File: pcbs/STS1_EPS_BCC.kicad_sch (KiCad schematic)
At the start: 45 parts, among them Q1 SI7135DP-T1-GE3, U1 LTC4020EUHFPBF, U2 SI7272DP-T1-GE3, U3 SI7272DP-T1-GE3

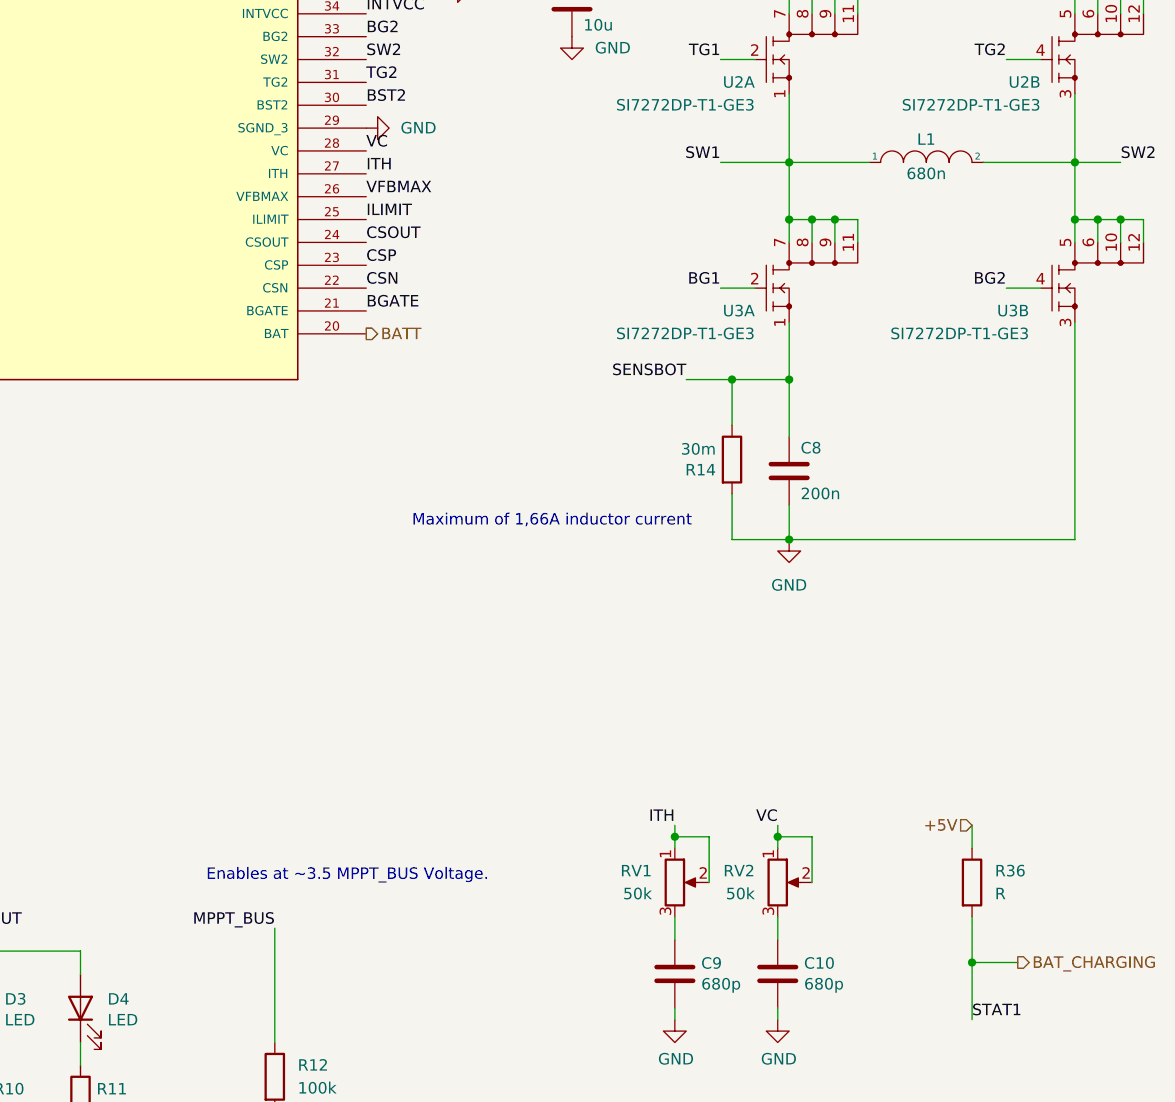
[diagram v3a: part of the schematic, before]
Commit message: Worked on STS1_EPS_1 and began work on STS1_EPS_2.
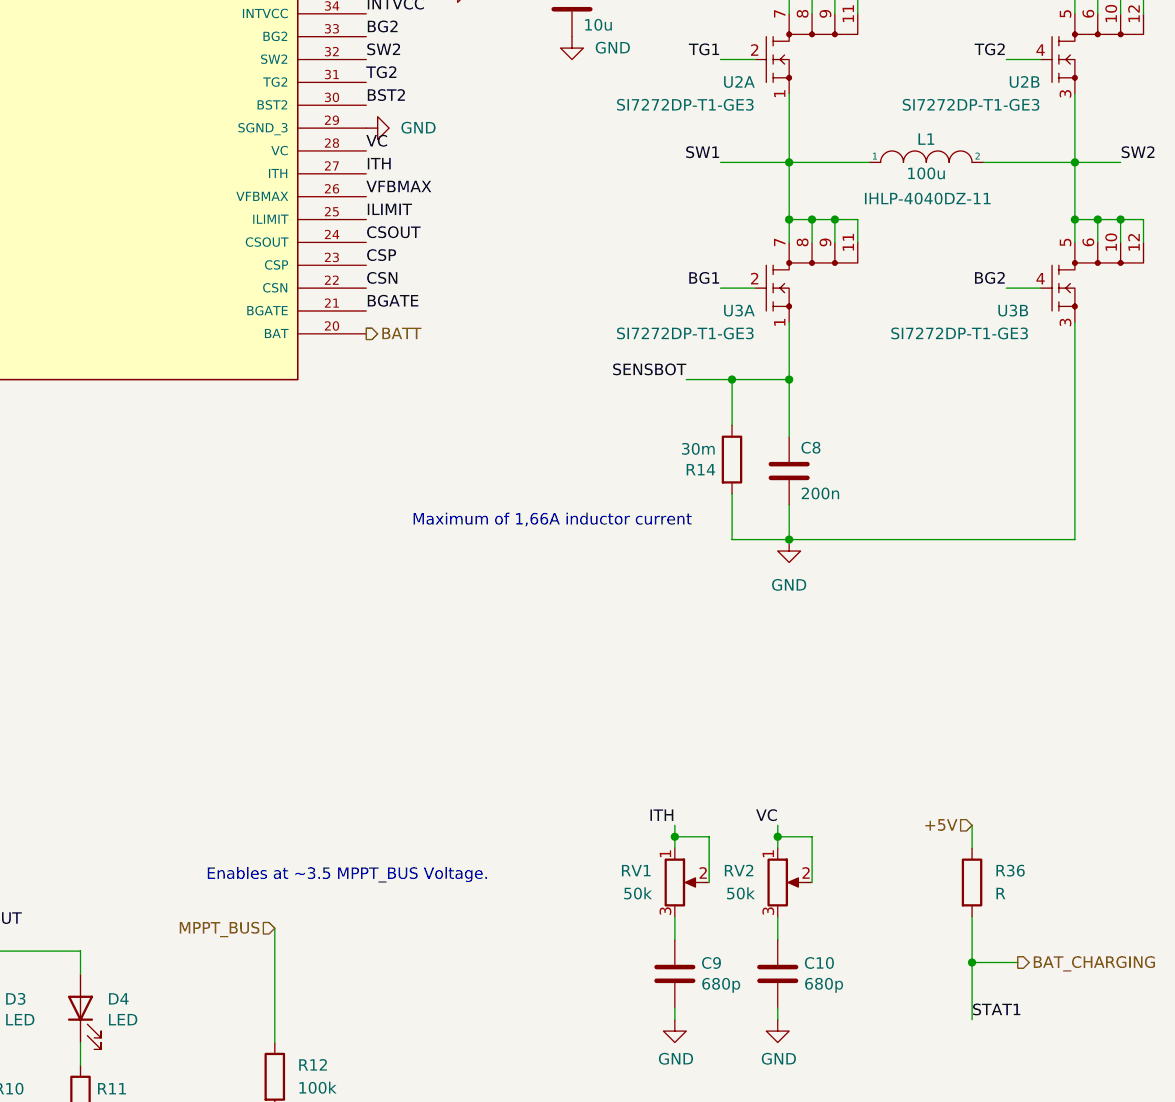
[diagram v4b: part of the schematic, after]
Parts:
- C32, C4: footprint (none) -> Capacitor_Tantalum_SMD:CP_EIA-7343-43_Kemet-X
- L1: value 680n -> 100u; footprint Inductor_SMD:L_10.4x10.4_H4.8 -> Inductor_SMD:L_Vishay_IHLP-4040; Part (none) -> IHLP-4040DZ-11
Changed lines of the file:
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@@
-    (effects (font (size 1.27 1.27)) (justify right bottom))
-  )
-  (label "MPPT_BUS" (at 135.89 148.59 180)
     (effects (font (size 1.27 1.27)) (justify right bottom))
   )
@@
   (label "VFBMAX" (at 146.05 67.31 0)
     (effects (font (size 1.27 1.27)) (justify left bottom))
+  )
+  (hierarchical_label "MPPT_BUS" (shape input) (at 135.89 148.59 180)
+    (effects (font (size 1.27 1.27)) (justify right))
   )
   (hierarchical_label "VOUT" (shape output) (at 275.59 16.51 0)
@@
     (in_bom yes) (on_board yes)
     (property "Reference" "L1" (id 0) (at 208.28 60.96 0))
-    (property "Value" "680n" (id 1) (at 208.28 64.77 0))
-    (property "Footprint" "Inductor_SMD:L_10.4x10.4_H4.8" (id 2) (at 208.28 63.5 0)
+    (property "Value" "100u" (id 1) (at 208.28 64.77 0))
+    (property "Footprint" "Inductor_SMD:L_Vishay_IHLP-4040" (id 2) (at 208.28 63.5 0)
       (effects (font (size 1.27 1.27)) hide)
     )
@@
       (effects (font (size 1.27 1.27)) hide)
     )
+    (property "Part" "IHLP-4040DZ-11" (id 4) (at 208.4324 67.564 0))
     (pin "1")
     (pin "2")
@@
       (effects (font (size 1.27 1.27)) (justify left))
     )
-    (property "Footprint" "" (id 2) (at 237.1852 24.13 0)
+    (property "Footprint" "Capacitor_Tantalum_SMD:CP_EIA-7343-43_Kemet-X" (id 2) (at 237.1852 24.13 0)
       (effects (font (size 1.27 1.27)) hide)
     )
@@
       (effects (font (size 1.27 1.27)) (justify left))
     )
-    (property "Footprint" "" (id 2) (at 33.9852 27.94 0)
-      (effects (font (size 1.27 1.27)) hide)
-    )
+    (property "Footprint" "Capacitor_Tantalum_SMD:CP_EIA-7343-43_Kemet-X" (id 2) (at 33.9852 27.94 0)
+      (effects (font (size 1.27 1.27)) hide)
+    )

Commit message: Finished first revision of schematic.
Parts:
- added R?: 100k, Resistor_SMD:R_0805_2012Metric, symbol Device:R
- R36: value R -> 100k
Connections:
- net +5V: now also R?.1
- net STAT2 renamed BAT_FAULT
- net BAT_FAULT: now also R?.2
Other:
- moved on the sheet: C33
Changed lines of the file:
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@@
   (junction (at 102.87 151.13) (diameter 0) (color 0 0 0 0)
   )
+  (junction (at 236.22 152.4) (diameter 0) (color 0 0 0 0)
+  )
   (junction (at 229.87 44.45) (diameter 0) (color 0 0 0 0)
   )
@@
     (stroke (width 0) (type default) (color 0 0 0 0))
   )
+  (wire (pts (xy 236.22 147.32) (xy 236.22 152.4))
+    (stroke (width 0) (type default) (color 0 0 0 0))
+  )
   (wire (pts (xy 270.51 36.83) (xy 273.05 36.83))
     (stroke (width 0) (type default) (color 0 0 0 0))
@@
     (stroke (width 0) (type default) (color 0 0 0 0))
   )
+  (wire (pts (xy 236.22 152.4) (xy 241.3 152.4))
+    (stroke (width 0) (type default) (color 0 0 0 0))
+  )
   (wire (pts (xy 265.43 34.29) (xy 267.97 34.29))
     (stroke (width 0) (type default) (color 0 0 0 0))
@@
     (stroke (width 0) (type default) (color 0 0 0 0))
   )
-  (wire (pts (xy 248.92 137.16) (xy 248.92 144.78))
+  (wire (pts (xy 271.78 137.16) (xy 271.78 144.78))
     (stroke (width 0) (type default) (color 0 0 0 0))
   )
@@
     (stroke (width 0) (type default) (color 0 0 0 0))
   )
-  (wire (pts (xy 248.92 152.4) (xy 248.92 158.75))
+  (wire (pts (xy 271.78 152.4) (xy 271.78 158.75))
     (stroke (width 0) (type default) (color 0 0 0 0))
   )
@@
     (stroke (width 0) (type default) (color 0 0 0 0))
   )
+  (wire (pts (xy 236.22 152.4) (xy 236.22 158.75))
+    (stroke (width 0) (type default) (color 0 0 0 0))
+  )
   (wire (pts (xy 39.37 173.99) (xy 39.37 175.26))
     (stroke (width 0) (type default) (color 0 0 0 0))
@@
   )
   (wire (pts (xy 29.21 173.99) (xy 25.4 173.99))
+    (stroke (width 0) (type default) (color 0 0 0 0))
+  )
+  (wire (pts (xy 236.22 137.16) (xy 236.22 139.7))
     (stroke (width 0) (type default) (color 0 0 0 0))
   )
@@
     (effects (font (size 1.27 1.27)) (justify left bottom))
   )
+  (label "STAT2" (at 236.22 158.75 0)
+    (effects (font (size 1.27 1.27)) (justify left bottom))
+  )
   (label "TG1" (at 185.42 52.07 180)
     (effects (font (size 1.27 1.27)) (justify right bottom))
@@
     (effects (font (size 1.27 1.27)) (justify left bottom))
   )
-  (label "CSOUT" (at 248.92 137.16 180)
+  (label "CSOUT" (at 271.78 137.16 180)
     (effects (font (size 1.27 1.27)) (justify right bottom))
   )
@@
     (effects (font (size 1.27 1.27)) (justify left))
   )
+  (hierarchical_label "BAT_FAULT" (shape output) (at 241.3 152.4 0)
+    (effects (font (size 1.27 1.27)) (justify left))
+  )
   (hierarchical_label "MPPT_BUS" (shape input) (at 25.4 16.51 180)
     (effects (font (size 1.27 1.27)) (justify right))
@@
   )
   (hierarchical_label "NTC" (shape input) (at 74.93 72.39 180)
+    (effects (font (size 1.27 1.27)) (justify right))
+  )
+  (hierarchical_label "+5V" (shape input) (at 236.22 137.16 180)
     (effects (font (size 1.27 1.27)) (justify right))
   )
@@
     )
     (pin "1")
+  )
+  (symbol (lib_id "Device:R") (at 236.22 143.51 0) (unit 1)
+    (in_bom yes) (on_board yes) (fields_autoplaced)
+    (property "Reference" "R?" (id 0) (at 238.76 142.2399 0)
+      (effects (font (size 1.27 1.27)) (justify left))
+    )
+    (property "Value" "100k" (id 1) (at 238.76 144.7799 0)
+      (effects (font (size 1.27 1.27)) (justify left))
+    )
+    (property "Footprint" "Resistor_SMD:R_0805_2012Metric" (id 2) (at 234.442 143.51 90)
+      (effects (font (size 1.27 1.27)) hide)
+    )
+    (property "Datasheet" "~" (id 3) (at 236.22 143.51 0)
+      (effects (font (size 1.27 1.27)) hide)
+    )
+    (pin "1")
+    (pin "2")
   )
   (symbol (lib_id "Device:R") (at 186.69 96.52 0) (unit 1)
@@
     (pin "2")
   )
-  (symbol (lib_id "power:GND") (at 248.92 158.75 0) (unit 1)
-    (in_bom yes) (on_board yes)
-    (property "Reference" "#PWR093" (id 0) (at 248.92 165.1 0)
-      (effects (font (size 1.27 1.27)) hide)
-    )
-    (property "Value" "GND" (id 1) (at 249.047 163.1442 0))
-    (property "Footprint" "" (id 2) (at 248.92 158.75 0)
-      (effects (font (size 1.27 1.27)) hide)
-    )
-    (property "Datasheet" "" (id 3) (at 248.92 158.75 0)
+  (symbol (lib_id "power:GND") (at 271.78 158.75 0) (unit 1)
+    (in_bom yes) (on_board yes)
+    (property "Reference" "#PWR093" (id 0) (at 271.78 165.1 0)
+      (effects (font (size 1.27 1.27)) hide)
+    )
+    (property "Value" "GND" (id 1) (at 271.907 163.1442 0))
+    (property "Footprint" "" (id 2) (at 271.78 158.75 0)
+      (effects (font (size 1.27 1.27)) hide)
+    )
+    (property "Datasheet" "" (id 3) (at 271.78 158.75 0)
       (effects (font (size 1.27 1.27)) hide)
     )
@@
     (pin "2")
   )
-  (symbol (lib_id "Device:C") (at 248.92 148.59 0) (unit 1)
-    (in_bom yes) (on_board yes)
-    (property "Reference" "C33" (id 0) (at 251.841 147.4216 0)
-      (effects (font (size 1.27 1.27)) (justify left))
-    )
-    (property "Value" "100p" (id 1) (at 251.841 149.733 0)
-      (effects (font (size 1.27 1.27)) (justify left))
-    )
-    (property "Footprint" "Capacitor_SMD:C_0805_2012Metric" (id 2) (at 249.8852 152.4 0)
-      (effects (font (size 1.27 1.27)) hide)
-    )
-    (property "Datasheet" "~" (id 3) (at 248.92 148.59 0)
+  (symbol (lib_id "Device:C") (at 271.78 148.59 0) (unit 1)
+    (in_bom yes) (on_board yes)
+    (property "Reference" "C33" (id 0) (at 274.701 147.4216 0)
+      (effects (font (size 1.27 1.27)) (justify left))
+    )
+    (property "Value" "100p" (id 1) (at 274.701 149.733 0)
+      (effects (font (size 1.27 1.27)) (justify left))
+    )
+    (property "Footprint" "Capacitor_SMD:C_0805_2012Metric" (id 2) (at 272.7452 152.4 0)
+      (effects (font (size 1.27 1.27)) hide)
+    )
+    (property "Datasheet" "~" (id 3) (at 271.78 148.59 0)
       (effects (font (size 1.27 1.27)) hide)
     )
@@
       (effects (font (size 1.27 1.27)) (justify left))
     )
-    (property "Value" "R" (id 1) (at 215.9 144.7799 0)
-      (effects (font (size 1.27 1.27)) (justify left))
-    )
+    (property "Value" "100k" (id 1) (at 215.9 144.7799 0)
+      (effects (font (size 1.27 1.27)) (justify left))
+    )

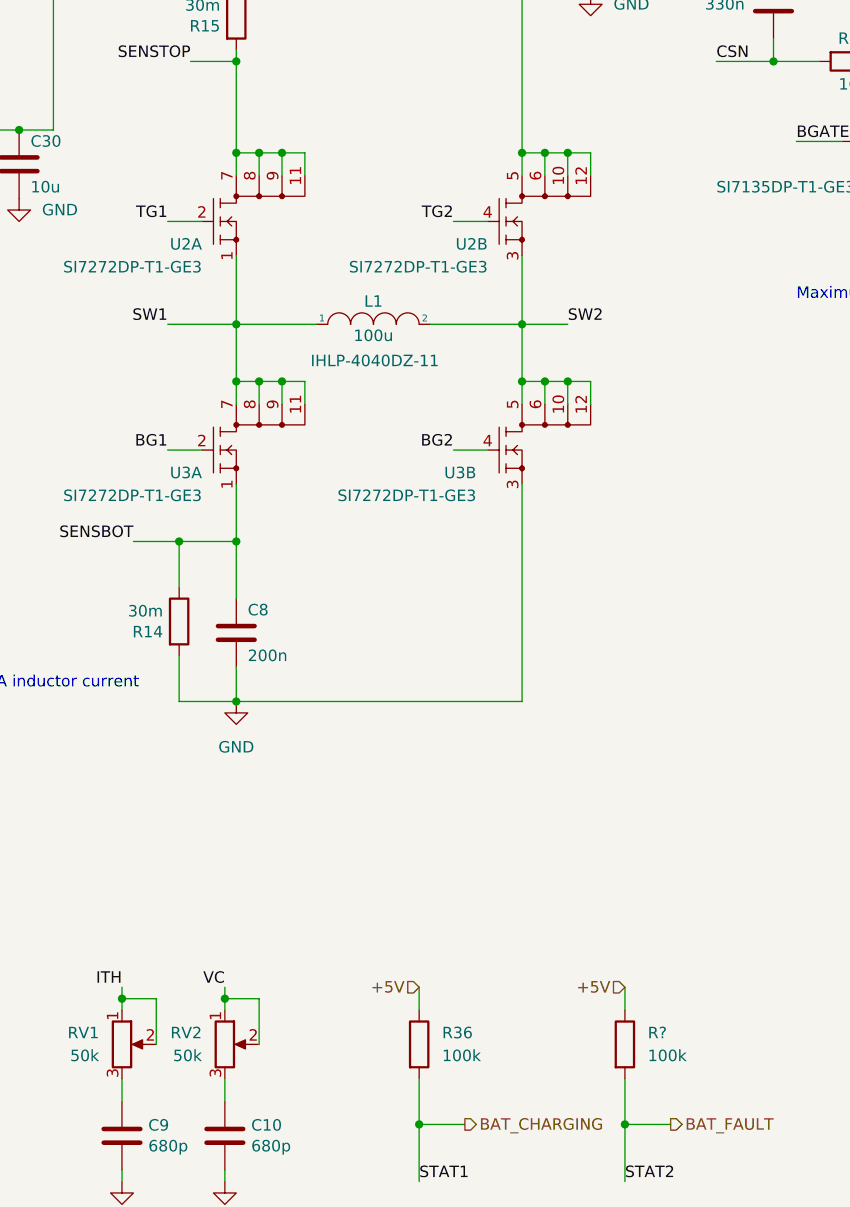
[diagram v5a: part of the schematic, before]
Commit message: Worked on STS1_EPS_2 layout.
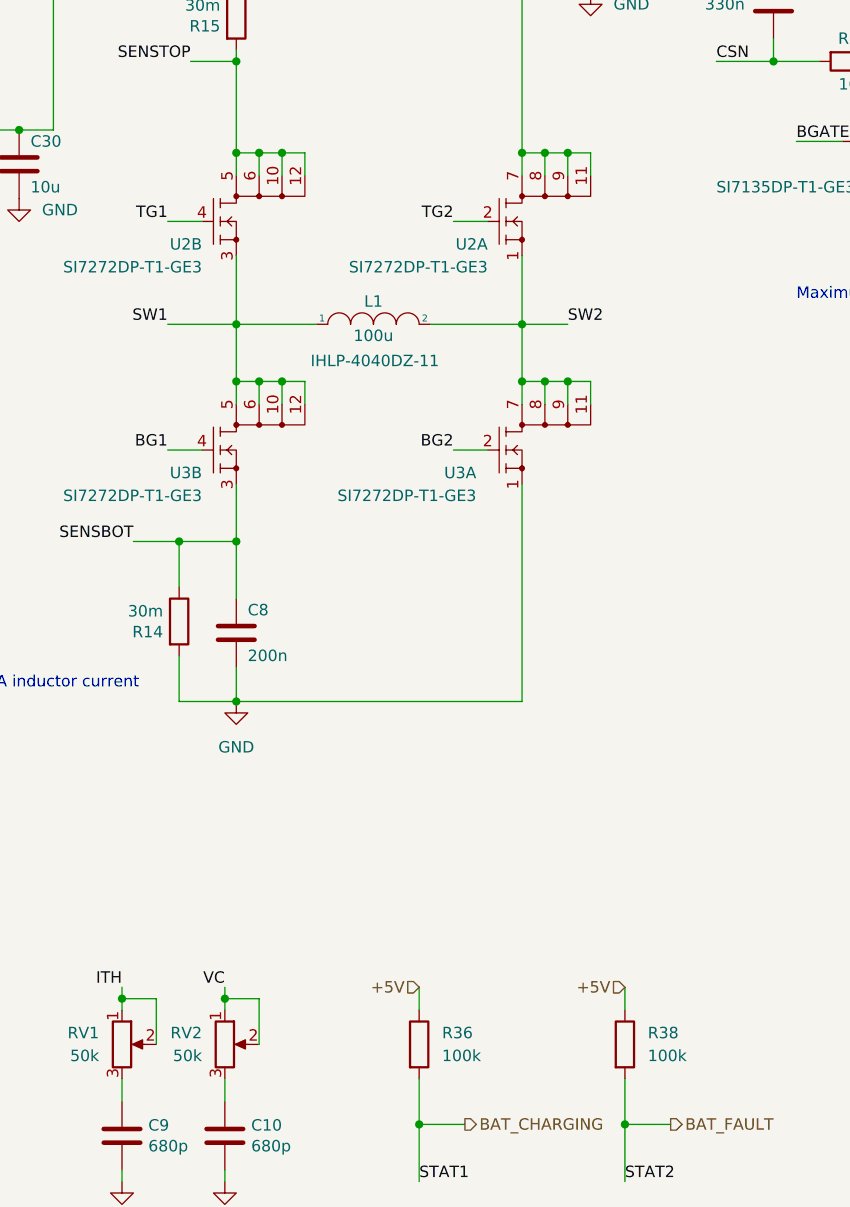
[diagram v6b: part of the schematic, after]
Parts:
- C8: footprint Capacitor_SMD:C_1812_4532Metric -> Capacitor_SMD:C_0805_2012Metric
- gave numbers to parts that had none: 1
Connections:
- net BG1: now also U3.4 (G2); no longer U3.2 (G1)
- net BG2: now also U3.2 (G1); no longer U3.4 (G2)
- net GND: now also U3.1 (S1); no longer U3.3 (S2)
- net SENSBOT: now also U3.3 (S2); no longer U3.1 (S1)
- net SENSTOP: now also U2.10 (D2_3), U2.12 (D2_4), U2.5 (D2_1), U2.6 (D2_2); no longer U2.11 (D1_4), U2.7 (D1_1), U2.8 (D1_2), U2.9 (D1_3)
- net SW1: now also U2.3 (S2), U3.10 (D2_3), U3.12 (D2_4), U3.5 (D2_1), U3.6 (D2_2); no longer U2.1 (S1), U3.11 (D1_4), U3.7 (D1_1), U3.8 (D1_2), U3.9 (D1_3)
- net SW2: now also U2.1 (S1), U3.11 (D1_4), U3.7 (D1_1), U3.8 (D1_2), U3.9 (D1_3); no longer U2.3 (S2), U3.10 (D2_3), U3.12 (D2_4), U3.5 (D2_1), U3.6 (D2_2)
- net TG1: now also U2.4 (G2); no longer U2.2 (G1)
- net TG2: now also U2.2 (G1); no longer U2.4 (G2)
- net VOUT: now also U2.11 (D1_4), U2.7 (D1_1), U2.8 (D1_2), U2.9 (D1_3); no longer U2.10 (D2_3), U2.12 (D2_4), U2.5 (D2_1), U2.6 (D2_2)
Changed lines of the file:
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@@
   (symbol (lib_id "Device:R") (at 236.22 143.51 0) (unit 1)
     (in_bom yes) (on_board yes) (fields_autoplaced)
-    (property "Reference" "R?" (id 0) (at 238.76 142.2399 0)
+    (property "Reference" "R38" (id 0) (at 238.76 142.2399 0)
       (effects (font (size 1.27 1.27)) (justify left))
     )
@@
     (pin "2")
   )
-  (symbol (lib_id "STS_Transistor_FET:SI7272DP-T1-GE3") (at 189.23 52.07 0) (unit 1)
+  (symbol (lib_id "STS_Transistor_FET:SI7272DP-T1-GE3") (at 189.23 52.07 0) (unit 2)
     (in_bom yes) (on_board yes)
     (property "Reference" "U2" (id 0) (at 189.23 54.61 0)
@@
       (effects (font (size 1.27 1.27)) (justify right))
     )
-    (property "Footprint" "Capacitor_SMD:C_1812_4532Metric" (id 2) (at 192.0748 93.98 0)
+    (property "Footprint" "Capacitor_SMD:C_0805_2012Metric" (id 2) (at 192.0748 93.98 0)
       (effects (font (size 1.27 1.27)) hide)
     )
@@
     (pin "2")
   )
-  (symbol (lib_id "STS_Transistor_FET:SI7272DP-T1-GE3") (at 189.23 77.47 0) (unit 1)
+  (symbol (lib_id "STS_Transistor_FET:SI7272DP-T1-GE3") (at 189.23 77.47 0) (unit 2)
     (in_bom yes) (on_board yes)
     (property "Reference" "U3" (id 0) (at 189.23 80.01 0)
@@
     (pin "1")
   )
-  (symbol (lib_id "STS_Transistor_FET:SI7272DP-T1-GE3") (at 220.98 52.07 0) (unit 2)
+  (symbol (lib_id "STS_Transistor_FET:SI7272DP-T1-GE3") (at 220.98 52.07 0) (unit 1)
     (in_bom yes) (on_board yes)
     (property "Reference" "U2" (id 0) (at 220.98 54.61 0)
@@
     (pin "2")
   )
-  (symbol (lib_id "STS_Transistor_FET:SI7272DP-T1-GE3") (at 220.98 77.47 0) (unit 2)
+  (symbol (lib_id "STS_Transistor_FET:SI7272DP-T1-GE3") (at 220.98 77.47 0) (unit 1)
     (in_bom yes) (on_board yes)
     (property "Reference" "U3" (id 0) (at 219.71 80.01 0)

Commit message: Worked on STS1_EPS_1 layout.
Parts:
- removed C7: 10µ, Capacitor_SMD:C_0805_2012Metric, symbol Device:C
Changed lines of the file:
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@@
-    (stroke (width 0) (type default) (color 0 0 0 0))
-  )
-  (wire (pts (xy 66.04 92.71) (xy 66.04 88.9))
     (stroke (width 0) (type default) (color 0 0 0 0))
   )
@@
   )
   (wire (pts (xy 52.07 92.71) (xy 52.07 88.9))
-    (stroke (width 0) (type default) (color 0 0 0 0))
-  )
-  (wire (pts (xy 66.04 100.33) (xy 66.04 102.87))
     (stroke (width 0) (type default) (color 0 0 0 0))
   )
@@
     (effects (font (size 1.27 1.27)) (justify right bottom))
   )
+  (label "PVIN" (at 146.05 41.91 0)
+    (effects (font (size 1.27 1.27)) (justify left bottom))
+  )
   (label "VFBMIN" (at 29.21 173.99 0)
     (effects (font (size 1.27 1.27)) (justify left bottom))
@@
   )
   (label "SW2" (at 15.24 107.95 0)
-    (effects (font (size 1.27 1.27)) (justify left bottom))
-  )
-  (label "PVIN" (at 66.04 88.9 0)
     (effects (font (size 1.27 1.27)) (justify left bottom))
   )
@@
     (pin "2")
   )
-  (symbol (lib_id "power:GND") (at 66.04 102.87 0) (unit 1)
-    (in_bom yes) (on_board yes)
-    (property "Reference" "#PWR06" (id 0) (at 66.04 109.22 0)
-      (effects (font (size 1.27 1.27)) hide)
-    )
-    (property "Value" "GND" (id 1) (at 66.167 107.2642 0))
-    (property "Footprint" "" (id 2) (at 66.04 102.87 0)
-      (effects (font (size 1.27 1.27)) hide)
-    )
-    (property "Datasheet" "" (id 3) (at 66.04 102.87 0)
-      (effects (font (size 1.27 1.27)) hide)
-    )
-    (pin "1")
-  )
   (symbol (lib_id "Device:C_Polarized") (at 236.22 20.32 0) (unit 1)
     (in_bom yes) (on_board yes) (fields_autoplaced)
@@
     (pin "1")
   )
-  (symbol (lib_id "Device:C") (at 66.04 96.52 180) (unit 1)
-    (in_bom yes) (on_board yes)
-    (property "Reference" "C7" (id 0) (at 72.4408 96.52 90))
-    (property "Value" "10µ" (id 1) (at 70.1294 96.52 90))
-    (property "Footprint" "Capacitor_SMD:C_0805_2012Metric" (id 2) (at 65.0748 92.71 0)
-      (effects (font (size 1.27 1.27)) hide)
-    )
-    (property "Datasheet" "~" (id 3) (at 66.04 96.52 0)
-      (effects (font (size 1.27 1.27)) hide)
-    )
-    (pin "1")
-    (pin "2")
-  )
   (symbol (lib_id "power:GND") (at 33.02 31.75 0) (unit 1)
